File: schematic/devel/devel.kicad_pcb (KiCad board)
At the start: 2 copper layers, 43 parts, among them J1 CONN_PWR, J2 CONN_X1, J3 CONN_X2, J4 CONN_Y1, J5 CONN_Y2, J6 CONN_PWR, U1 L7812, U2 L7912, U3 REF5010IDGK, U4 OPA4197

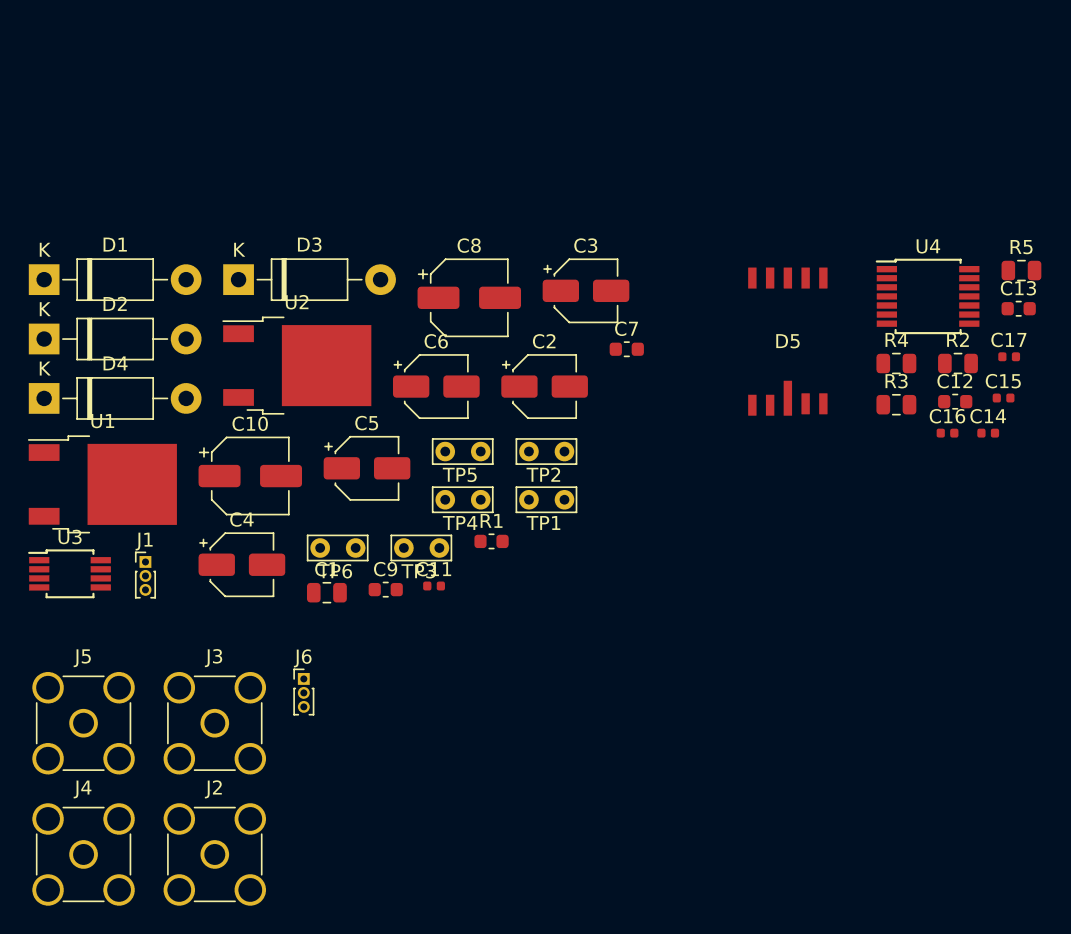
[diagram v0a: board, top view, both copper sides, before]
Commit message: merged circuit sheets to single sheet, removed extra diodes, changed diode type
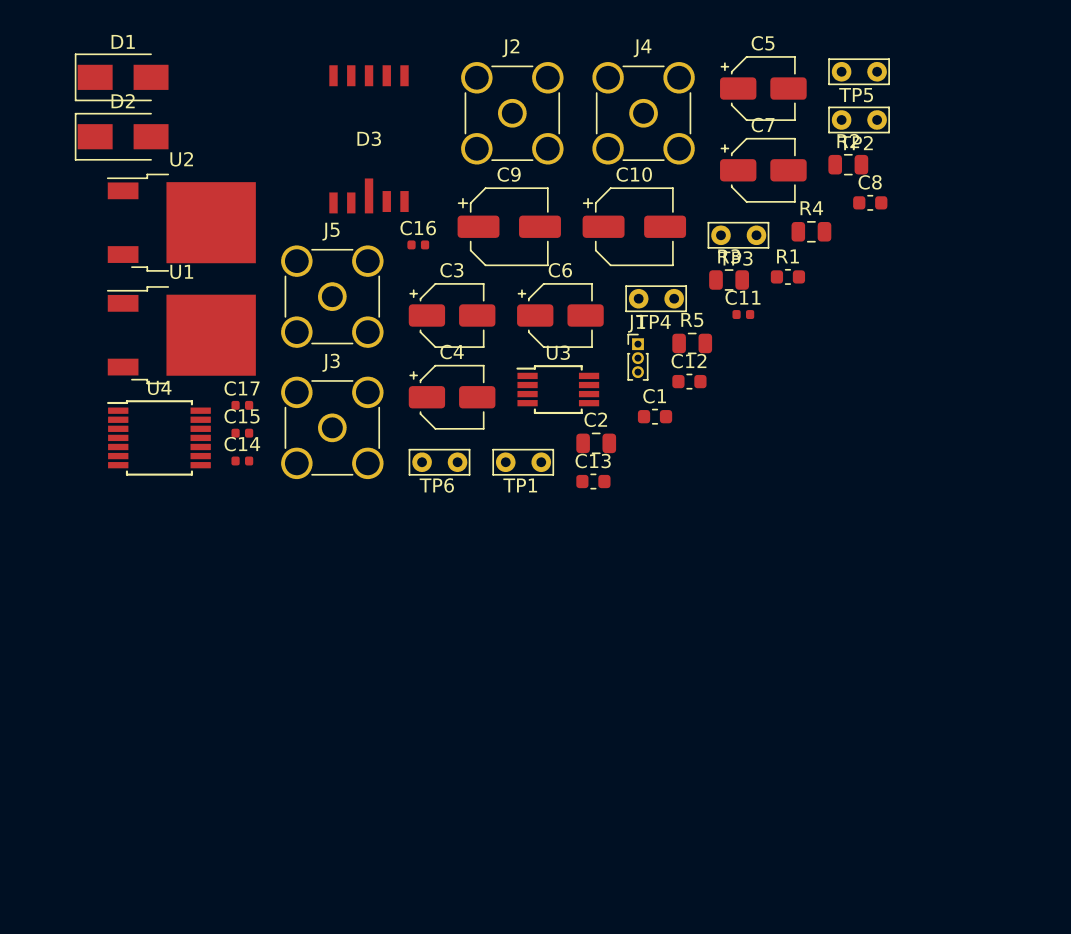
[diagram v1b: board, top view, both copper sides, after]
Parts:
- removed D4: 1N4001, Diode_THT:D_DO-41_SOD81_P10.16mm_Horizontal
- removed D5: S599x, Sensor_OpticalPosition:S5990
- removed J6: CONN_PWR, Connector_PinHeader_1.00mm:PinHeader_1x03_P1.00mm_Vertical
- C1: footprint Capacitor_SMD:C_0805_2012Metric -> Capacitor_SMD:C_0603_1608Metric
- C2: value 2.2u -> 330n; footprint Capacitor_SMD:CP_Elec_4x5.4 -> Capacitor_SMD:C_0805_2012Metric
- C3: value 10u -> 2.2u
- C5: value 1u -> 10u
- C7: value 100n -> 1u; footprint Capacitor_SMD:C_0603_1608Metric -> Capacitor_SMD:CP_Elec_4x5.4
- C8: value 1u -> 100n; footprint Capacitor_SMD:CP_Elec_5x4.4 -> Capacitor_SMD:C_0603_1608Metric
- C9: value 330n -> 1u; footprint Capacitor_SMD:C_0603_1608Metric -> Capacitor_SMD:CP_Elec_5x4.4
- D1, D2: value 1N4001 -> D_Schottky; footprint Diode_THT:D_DO-41_SOD81_P10.16mm_Horizontal -> Diode_SMD:D_SMA
- D3: value 1N4001 -> S599x; footprint Diode_THT:D_DO-41_SOD81_P10.16mm_Horizontal -> Sensor_OpticalPosition:S5990
- J3: value CONN_X2 -> CONN_Y2
- J4: value CONN_Y1 -> CONN_X2
- J5: value CONN_Y2 -> CONN_Y1
- moved J4 66.5 mm to (205.6, 36.7)
- moved J2 57.1 mm to (196.2, 36.7)
- moved U4 55.9 mm to (170.9, 59.9)
- moved C17 55.0 mm to (176.8, 57.6)
- moved C15 54.5 mm to (176.8, 59.6)
- moved C14 53.4 mm to (176.8, 61.6)
- moved C16 40.2 mm to (189.4, 46.1)
- moved C5 39.3 mm to (214.1, 34.9)
- moved TP5 39.3 mm to (219.7, 33.7)
- moved J1 38.5 mm to (205.2, 53.2)
- moved U3 37.3 mm to (199.5, 56.5)
- moved J5 35.3 mm to (183.3, 49.8)
- moved C13 32.8 mm to (202.0, 63.1)
- moved C10 32.8 mm to (204.9, 44.8)
- moved TP2 32.6 mm to (219.7, 37.2)
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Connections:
- net -X1 renamed Net-(C14-Pad2)
- net -Y2 renamed Net-(C17-Pad2)
- C10 pad 1: +10V -> Net-(C10-Pad1)
- C15 pad 2: -Y1 -> Net-(C15-Pad2)
- C16 pad 2: -X2 -> Net-(C16-Pad2)
- C2 pad 1: GND -> +15V
- C2 pad 2: -15V -> GND
- C3 pad 1: +15V -> GND
- C3 pad 2: GND -> -15V
- C4 pad 1: GND -> +15V
- C4 pad 2: -15V -> GND
- C5 pad 1: +15V -> GND
- C5 pad 2: GND -> -15V
- C6 pad 1: GND -> +15V
- C6 pad 2: -15V -> GND
- C7 pad 1: +12V -> GND
- C7 pad 2: GND -> -15V
- C8 pad 1: GND -> +12V
- C8 pad 2: -12V -> GND
- C9 pad 1: +15V -> GND
- C9 pad 2: GND -> -12V
- D1 pad 1: +15V -> +12V
- D1 pad 2: +12V -> GND
- D2 pad 1: -15V -> -12V
- D2 pad 2: -12V -> GND
- D3 pad 1: +12V -> Net-(C14-Pad1)
- D3 pad 2: GND -> (no net)
- J3 pad 1: -X2 -> Net-(C15-Pad2)
- J4 pad 1: -Y1 -> Net-(C16-Pad2)
- R1 pad 1: +10V -> Net-(C10-Pad1)
- R3 pad 2: -Y1 -> Net-(C15-Pad2)
- R4 pad 2: -X2 -> Net-(C16-Pad2)
- TP6 pad 1: +10V -> Net-(C10-Pad1)
- U3 pad 6: +10V -> Net-(C10-Pad1)
- U4 pad 14: -Y1 -> Net-(C15-Pad2)
- U4 pad 7: -X2 -> Net-(C16-Pad2)
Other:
- copper layers 2 -> 4

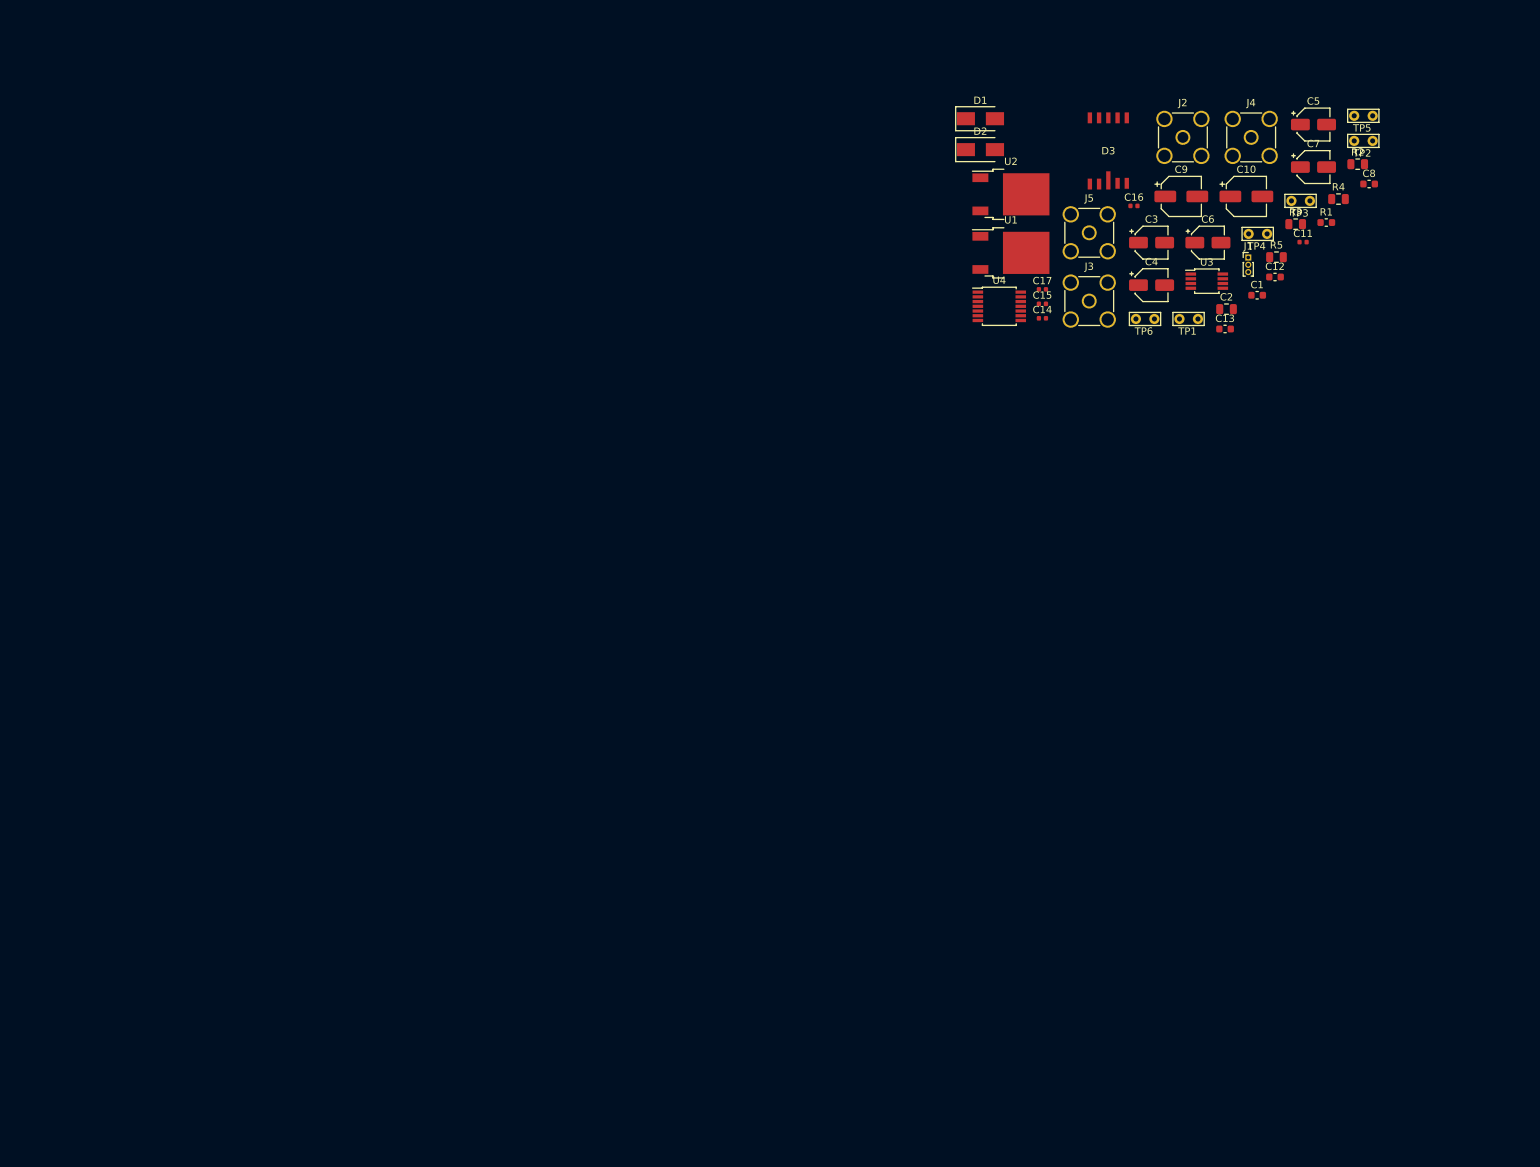
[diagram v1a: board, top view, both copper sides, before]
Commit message: reassigned footprints that were not smd compatible
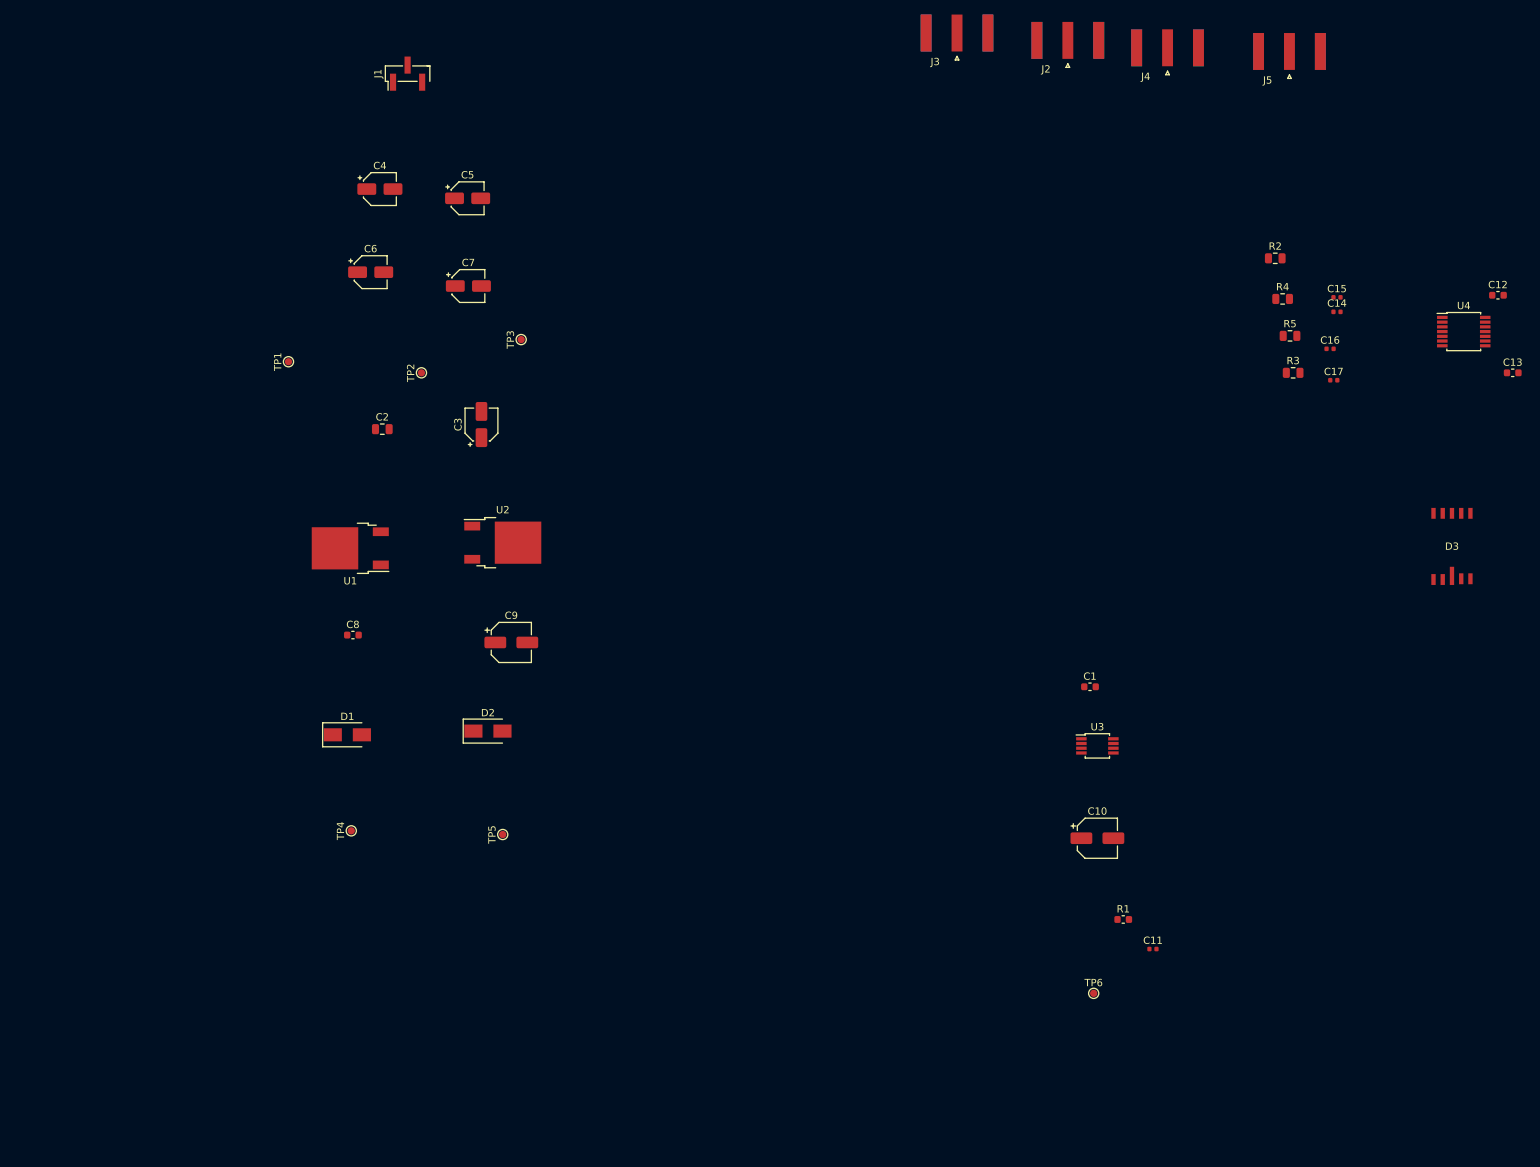
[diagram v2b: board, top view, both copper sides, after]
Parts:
- J1: footprint Connector_PinHeader_1.00mm:PinHeader_1x03_P1.00mm_Vertical -> Connector_PinHeader_2.00mm:PinHeader_1x03_P2.00mm_Vertical_SMD_Pin1Left
- J2, J3, J4, J5: footprint Connector_Coaxial:SMA_Amphenol_901-144_Vertical -> Connector_Coaxial:SMA_Amphenol_132289_EdgeMount
- TP1, TP2, TP3, TP4, TP5, TP6: footprint TestPoint:TestPoint_Bridge_Pitch2.54mm_Drill0.7mm -> TestPoint:TestPoint_Pad_D1.0mm
- moved TP5 153.2 mm to (102.6, 132.6), turned to 90 degrees
- moved C8 152.9 mm to (82.0, 105.2)
- moved TP4 148.2 mm to (81.8, 132.1), turned to 90 degrees
- moved TP2 132.2 mm to (91.4, 69.1), turned to 90 degrees
- moved TP1 122.7 mm to (73.2, 67.6), turned to 90 degrees
- moved D1 121.5 mm to (81.2, 118.9)
- moved J1 118.4 mm to (89.5, 27.9), turned to 90 degrees
- moved C7 117.4 mm to (97.9, 57.1)
- moved C2 117.3 mm to (86.1, 76.8)
- moved C5 116.8 mm to (97.8, 45.1)
- moved C6 115.2 mm to (84.5, 55.2)
- moved C9 110.7 mm to (103.8, 106.2)
- moved TP3 107.6 mm to (105.2, 64.5), turned to 90 degrees
- moved C4 106.9 mm to (85.7, 43.8)
- moved D2 104.8 mm to (100.6, 118.4)
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
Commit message: created first pcb layout draft
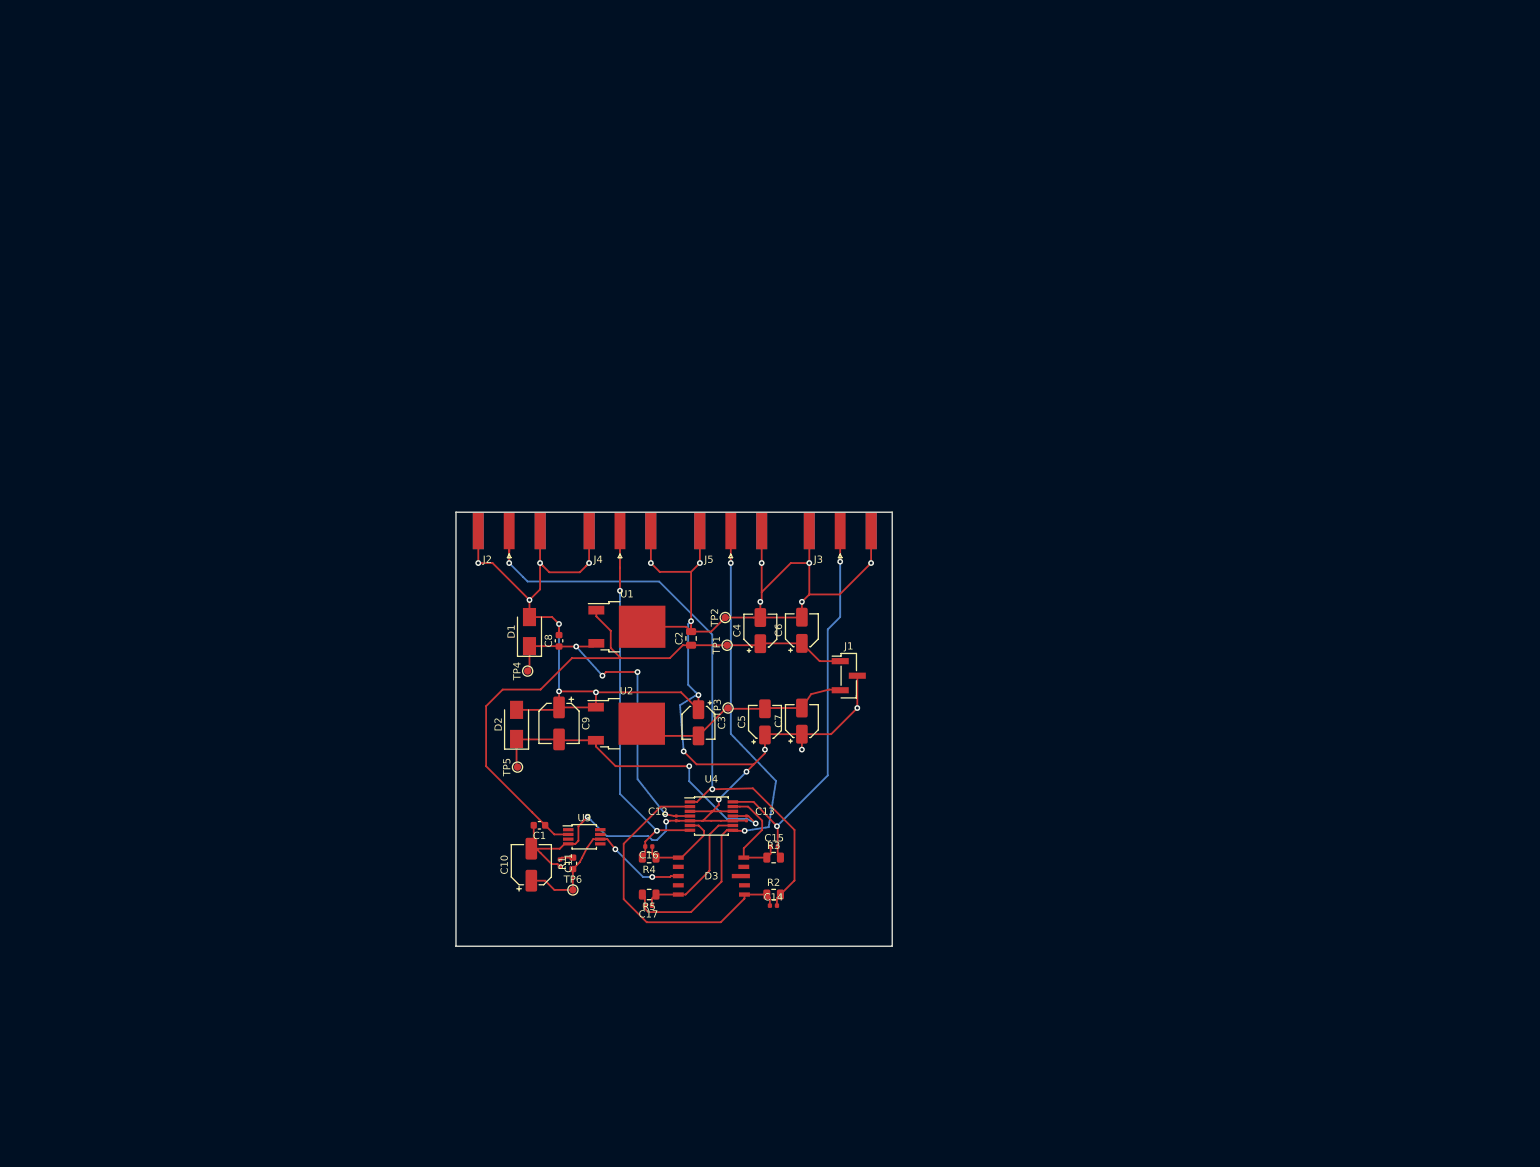
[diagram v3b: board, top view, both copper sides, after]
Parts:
- C12, C13: footprint Capacitor_SMD:C_0603_1608Metric -> Capacitor_SMD:C_0201_0603Metric
- moved C12 134.0 mm to (126.5, 130.4), turned to 90 degrees
- moved U4 123.1 mm to (131.3, 130.0)
- moved C13 121.9 mm to (136.1, 130.4), turned to 90 degrees
- moved C17 118.8 mm to (122.7, 142.4), turned to 180 degrees
- moved R5 116.9 mm to (122.8, 140.8), turned to 180 degrees
- moved R4 116.2 mm to (122.8, 135.8), turned to 180 degrees
- moved C16 116.0 mm to (122.7, 134.2), turned to 180 degrees
- moved C14 112.6 mm to (139.8, 142.4)
- moved D3 111.5 mm to (131.3, 138.3), turned to 90 degrees
- moved R2 111.4 mm to (139.9, 140.8)
- moved C15 108.1 mm to (140.0, 134.2)
- moved J1 102.7 mm to (150.2, 110.7), turned to 0 degrees
- moved J2 102.2 mm to (103.5, 90.8)
- moved J5 101.2 mm to (134.0, 90.8)
- moved J4 100.4 mm to (118.7, 90.8)
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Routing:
- net GND: track 0.00 -> 302.4 mm, vias 0 -> 24
- net Net-(C14-Pad2): track 0.00 -> 93.2 mm, vias 0 -> 2
- net +15V: track 0.00 -> 84.7 mm
- net Net-(C17-Pad2): track 0.00 -> 71.1 mm, vias 0 -> 2
- net Net-(C15-Pad2): track 0.00 -> 56.3 mm, vias 0 -> 2
- net Net-(C16-Pad2): track 0.00 -> 52.5 mm, vias 0 -> 2
- net +12V: track 0.00 -> 47.7 mm, vias 0 -> 4
- net -12V: track 0.00 -> 46.8 mm, vias 0 -> 2
- net Net-(C14-Pad1): track 0.00 -> 43.5 mm
- net Net-(C10-Pad1): track 0.00 -> 28.4 mm, vias 0 -> 2
- net -15V: track 0.00 -> 27.4 mm
- net Net-(C17-Pad1): track 0.00 -> 19.2 mm
- net Net-(C15-Pad1): track 0.00 -> 15.9 mm
- net Net-(C16-Pad1): track 0.00 -> 12.5 mm
- net Net-(C11-Pad1): track 0.00 -> 1.88 mm
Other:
- board outline added: 60 x 59.7 mm
- copper layers 4 -> 2
- net class Power added: clearance 0.5, trace_width 1, via_dia 0.8, via_drill 0.4
